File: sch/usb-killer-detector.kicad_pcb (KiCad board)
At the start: 2 copper layers, 44 x 82 mm, 35 parts, among them J1 USB_A, J2 USB_C_Receptacle_PowerOnly_6P, Q2 2N3904, U1 LM339

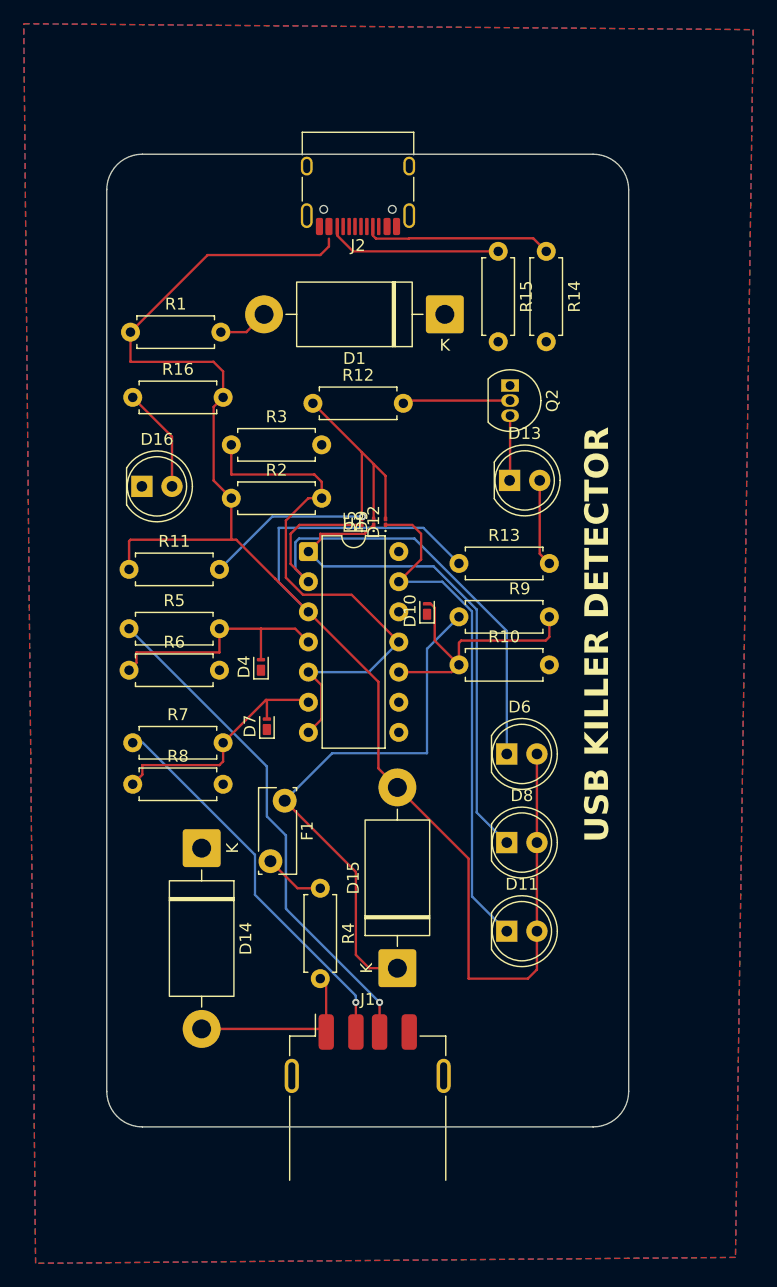
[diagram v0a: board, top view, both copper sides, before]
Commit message: Reprise v2 : schéma refait, PCB routé et dossier de fabrication
- Détection des deux polarités sur D+, D- et VBUS : comparateurs à
  fenêtre (2x LM339), seuils D+/D- +6,2 V / -5,0 V, VBUS +6,3 V / -0,3 V
- Alerte mémorisée (74HC279) avec bouton RESET et reset à la mise
  sous tension ; LED verte « OK » quand aucune alerte
- Protections : TVS SMAJ5.0A, clamps BAT54S, diode anti-retour SS34,
  polyfuse 500 mA
- PCB 44 x 82 mm entièrement routé, plans de masse sur les deux faces
- Règles d'isolation des lignes haute tension (kicad_dru) et classes
  de pistes (Power, HV)
- ERC 0, DRC 0 : les 2 avertissements de sérigraphie du connecteur
  USB-A (corps hors carte par construction) sont exclus avec justification
- sch/fabrication : Gerber + perçage (zip prêt à envoyer), BOM,
  fichier de placement, schéma et plan d'assemblage en PDF
- .gitignore : historique local de KiCad 10 (.history/)

Co-Authored-By: Claude Opus 5.5 <noreply@anthropic.com>
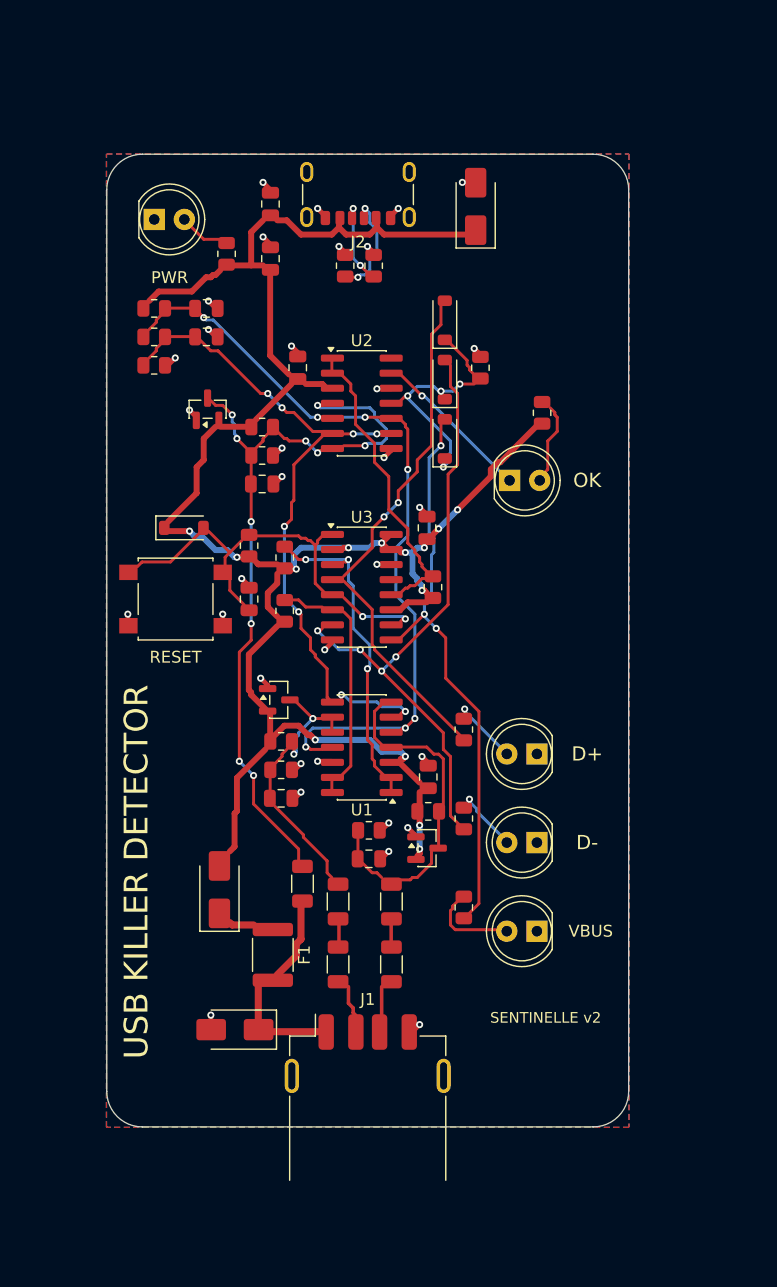
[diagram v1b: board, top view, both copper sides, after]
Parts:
- removed D16: LED_O, LED_THT:LED_D5.0mm
- removed Q2: 2N3904, Package_TO_SOT_THT:TO-92_Inline
- added C1: 10uF, Capacitor_SMD:C_0805_2012Metric, F.Cu at (80.3, 62.2)
- added C10: 100nF, Capacitor_SMD:C_0805_2012Metric, F.Cu at (93.5, 89.5)
- added C11: 1uF, Capacitor_SMD:C_0805_2012Metric, F.Cu at (78.5, 95.5)
- added C2: 100nF, Capacitor_SMD:C_0805_2012Metric, F.Cu at (80.3, 66.8)
- added C3: 100nF, Capacitor_SMD:C_0805_2012Metric, F.Cu at (74.9, 71.0)
- added C4: 100nF, Capacitor_SMD:C_0805_2012Metric, F.Cu at (74.9, 73.4)
- added C5: 1nF, Capacitor_SMD:C_0805_2012Metric, F.Cu at (88.6, 117.4)
- added C6: 1nF, Capacitor_SMD:C_0805_2012Metric, F.Cu at (81.2, 112.3)
- added C7: 1nF, Capacitor_SMD:C_0805_2012Metric, F.Cu at (79.6, 85.8)
- added C8: 100nF, Capacitor_SMD:C_0805_2012Metric, F.Cu at (93.6, 110.5)
- added C9: 100nF, Capacitor_SMD:C_0805_2012Metric, F.Cu at (82.6, 76.0)
- added D2: Orange PWR, LED_THT:LED_D5.0mm, F.Cu at (70.5, 63.5)
- added D3: SS34, Diode_SMD:D_SMA, F.Cu at (76.0, 120.0)
- added R17: 43k, Resistor_SMD:R_0805_2012Metric, F.Cu at (79.6, 83.4)
- added R18: 10k, Resistor_SMD:R_0805_2012Metric, F.Cu at (81.5, 92.0)
- added R19: 10k, Resistor_SMD:R_0805_2012Metric, F.Cu at (81.5, 96.5)
- added R20: 10k, Resistor_SMD:R_0805_2012Metric, F.Cu at (94.0, 94.5)
- added R21: 100k, Resistor_SMD:R_0805_2012Metric, F.Cu at (78.5, 91.0)
- added R22: 1k, Resistor_SMD:R_0805_2012Metric, F.Cu at (96.6, 106.5)
- added R23: 1k, Resistor_SMD:R_0805_2012Metric, F.Cu at (96.6, 114.0)
- added R24: 1k, Resistor_SMD:R_0805_2012Metric, F.Cu at (96.6, 121.5)
- added R25: 100k, Resistor_SMD:R_0805_2012Metric, F.Cu at (98.0, 76.0)
- added R26: 1k, Resistor_SMD:R_0805_2012Metric, F.Cu at (103.2, 79.8)
- added SW1: RESET, Button_Switch_SMD:SW_SPST_B3S-1000, F.Cu at (72.3, 95.5)
- added U2: LM339, Package_SO:SOIC-14_3.9x8.7mm_P1.27mm, F.Cu at (88.0, 79.0)
- added U3: 74HC279, Package_SO:SOIC-16_3.9x9.9mm_P1.27mm, F.Cu at (88.0, 94.5)
- D1: value D_Schottky -> SMAJ5.0A; footprint Diode_THT:D_DO-201AD_P15.24mm_Horizontal -> Diode_SMD:D_SMA
- D10: value PTVS7V5Z1USK -> Rouge D-; footprint Diode_SMD:Nexperia_DSN1608-2_1.6x0.8mm -> LED_THT:LED_D5.0mm
- D11: value LED_R_D- -> Rouge VBUS
- D12: value PTVS7V5Z1USK -> 1N4148W; footprint Diode_SMD:D_01005_0402Metric -> Diode_SMD:D_SOD-123
- D13: value LED_G -> 1N4148W; footprint LED_THT:LED_D5.0mm -> Diode_SMD:D_SOD-123
- D14: value D_Schottky -> 1N4148W; footprint Diode_THT:D_DO-201AD_P15.24mm_Horizontal -> Diode_SMD:D_SOD-123
- D15: value D_Schottky -> Verte OK; footprint Diode_THT:D_DO-201AD_P15.24mm_Horizontal -> LED_THT:LED_D5.0mm
- D4: value PTVS7V5Z1USK -> SMAJ5.0A; footprint Diode_SMD:Nexperia_DSN1608-2_1.6x0.8mm -> Diode_SMD:D_SMA
- D5: value PTVS7V5Z1USK -> BAT54S; footprint Diode_SMD:D_01005_0402Metric -> Package_TO_SOT_SMD:SOT-23
- D6: value LED_R_D+ -> BAT54S; footprint LED_THT:LED_D5.0mm -> Package_TO_SOT_SMD:SOT-23
- D7: value PTVS7V5Z1USK -> BAT54S; footprint Diode_SMD:Nexperia_DSN1608-2_1.6x0.8mm -> Package_TO_SOT_SMD:SOT-23
- D8: value LED_R_D- -> 1N4148W; footprint LED_THT:LED_D5.0mm -> Diode_SMD:D_SOD-123
- D9: value PTVS7V5Z1USK -> Rouge D+; footprint Diode_SMD:D_01005_0402Metric -> LED_THT:LED_D5.0mm
- F1: value Polyfuse 250-500mA -> 500mA hold; footprint Fuse:Fuse_Bourns_MF-RG300 -> Fuse:Fuse_1812_4532Metric
- J1: value USB_A -> USB-A test
- J2: value USB_C_Receptacle_PowerOnly_6P -> USB-C alim; footprint Connector_USB:USB_C_Receptacle_HRO_TYPE-C-31-M-12 -> Connector_USB:USB_C_Receptacle_GCT_USB4125-xx-x_6P_TopMnt_Horizontal
- R1: value 1K -> 5.1k; footprint Resistor_THT:R_Axial_DIN0207_L6.3mm_D2.5mm_P7.62mm_Horizontal -> Resistor_SMD:R_0805_2012Metric
- R10: value 22K -> 120k; footprint Resistor_THT:R_Axial_DIN0207_L6.3mm_D2.5mm_P7.62mm_Horizontal -> Resistor_SMD:R_0805_2012Metric
- R11, R7: value 100K -> 220k; footprint Resistor_THT:R_Axial_DIN0207_L6.3mm_D2.5mm_P7.62mm_Horizontal -> Resistor_SMD:R_1206_3216Metric
- R12: value 47K -> 220k; footprint Resistor_THT:R_Axial_DIN0207_L6.3mm_D2.5mm_P7.62mm_Horizontal -> Resistor_SMD:R_1206_3216Metric
- R13: value 100K -> 220k; footprint Resistor_THT:R_Axial_DIN0207_L6.3mm_D2.5mm_P7.62mm_Horizontal -> Resistor_SMD:R_0805_2012Metric
- R14: value 5k -> 120k; footprint Resistor_THT:R_Axial_DIN0207_L6.3mm_D2.5mm_P7.62mm_Horizontal -> Resistor_SMD:R_0805_2012Metric
- R15: value 5k -> 100k; footprint Resistor_THT:R_Axial_DIN0207_L6.3mm_D2.5mm_P7.62mm_Horizontal -> Resistor_SMD:R_1206_3216Metric
- R16: value 10K -> 150k; footprint Resistor_THT:R_Axial_DIN0207_L6.3mm_D2.5mm_P7.62mm_Horizontal -> Resistor_SMD:R_0805_2012Metric
- R2: value 36K -> 5.1k; footprint Resistor_THT:R_Axial_DIN0207_L6.3mm_D2.5mm_P7.62mm_Horizontal -> Resistor_SMD:R_0805_2012Metric
- R3: value 10K -> 1k; footprint Resistor_THT:R_Axial_DIN0207_L6.3mm_D2.5mm_P7.62mm_Horizontal -> Resistor_SMD:R_0805_2012Metric
- R4: value 22 -> 51k; footprint Resistor_THT:R_Axial_DIN0207_L6.3mm_D2.5mm_P7.62mm_Horizontal -> Resistor_SMD:R_0805_2012Metric
- R5: value 100K -> 33k; footprint Resistor_THT:R_Axial_DIN0207_L6.3mm_D2.5mm_P7.62mm_Horizontal -> Resistor_SMD:R_0805_2012Metric
- R6: value 22K -> 15k; footprint Resistor_THT:R_Axial_DIN0207_L6.3mm_D2.5mm_P7.62mm_Horizontal -> Resistor_SMD:R_0805_2012Metric
- R8: value 22K -> 220k; footprint Resistor_THT:R_Axial_DIN0207_L6.3mm_D2.5mm_P7.62mm_Horizontal -> Resistor_SMD:R_1206_3216Metric
- R9: value 390K -> 220k; footprint Resistor_THT:R_Axial_DIN0207_L6.3mm_D2.5mm_P7.62mm_Horizontal -> Resistor_SMD:R_0805_2012Metric
- U1: footprint Package_DIP:DIP-14_W7.62mm -> Package_SO:SOIC-14_3.9x8.7mm_P1.27mm
- moved R15 55.8 mm to (83.0, 119.5), turned to 90 degrees
- moved R4 50.8 mm to (70.5, 71.0), turned to 0 degrees
- moved R14 49.1 mm to (81.2, 109.9), turned to 0 degrees
- moved D15 42.2 mm to (100.5, 85.5), turned to 0 degrees
- moved R12 42.1 mm to (86.0, 121.0), turned to 90 degrees
- moved D14 40.1 mm to (95.0, 82.0), turned to 90 degrees
- moved D8 38.0 mm to (73.0, 89.5)
- moved R11 37.7 mm to (86.0, 126.3), turned to 90 degrees
- moved D4 30.7 mm to (77.3, 131.8), turned to 180 degrees
- moved R7 28.7 mm to (90.5, 126.3), turned to 90 degrees
- moved D5 28.0 mm to (93.5, 116.5), turned to 0 degrees
- moved D7 27.2 mm to (75.0, 79.5)
- moved R6 25.8 mm to (70.5, 75.8)
- moved R5 24.7 mm to (70.5, 73.4)
- moved R8 23.9 mm to (90.5, 121.0), turned to 90 degrees
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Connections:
- D1 pad 1: GND -> +5V
- D1 pad 2: Net-(D1-A) -> GND
- D10 pad 2: Net-(D10-A) -> /LED_DM
- D11 pad 1: Net-(D11-K) -> GND
- D11 pad 2: 5V -> /LED_VBUS
- D12 pad 1: Net-(D11-K) -> /ANY_ALM
- D12 pad 2: Net-(D12-A) -> /Q_DP
- D13 pad 1: Net-(D13-K) -> /ANY_ALM
- D13 pad 2: Net-(D13-A) -> /Q_DM
- D14 pad 1: GND -> /ANY_ALM
- D14 pad 2: VBUS -> /Q_VBUS
- D15 pad 1: VBUS_TEST -> /LED_OK_K
- D15 pad 2: 5V -> /LED_OK_A
- D4 pad 1: GND -> /VBUS_PORT
- D4 pad 2: Net-(D4-A) -> GND
- D5 pad 1: Net-(D5-K) -> GND
- D5 pad 2: Net-(D12-A) -> +5V
- D6 pad 1: Net-(D5-K) -> GND
- D6 pad 2: 5V -> +5V
- D7 pad 2: Net-(D7-A) -> +5V
- D8 pad 1: Net-(D8-K) -> +5V
- D8 pad 2: 5V -> /RST_N
- D9 pad 1: Net-(D8-K) -> GND
- D9 pad 2: Net-(D12-A) -> /LED_DP
- F1 pad 1: VBUS_TEST -> /VBUS_SRC
- F1 pad 2: Net-(F1-Pad2) -> /VBUS_PORT
- J1 pad 1: VBUS -> /VBUS_PORT
- J1 pad 2: D- -> /DM
- J1 pad 3: D+ -> /DP
- J1 pad SH: unconnected-(J1-Shield-PadSH) -> GND
- J2 pad A5: Net-(J2-CC1) -> /CC1
- J2 pad A9: 5V -> +5V
- J2 pad B5: Net-(J2-CC2) -> /CC2
- J2 pad B9: 5V -> +5V
- J2 pad SH: unconnected-(J2-SHIELD-PadSH) -> GND
- R1 pad 1: 5V -> /CC1
- R1 pad 2: Net-(D1-A) -> GND
- R10 pad 1: Net-(D10-A) -> /X_DP
- R11 pad 1: 5V -> /DM
- R11 pad 2: Net-(D12-A) -> /DM_HV
- R12 pad 1: Net-(D12-A) -> /DM_HV
- R12 pad 2: Net-(Q2-B) -> /X_DM
- R13 pad 1: 5V -> +5V
- R13 pad 2: Net-(D13-A) -> /X_DM
- R14 pad 1: Net-(J2-CC1) -> /X_DM
- R15 pad 1: Net-(J2-CC2) -> /VBUS_PORT
- R15 pad 2: GND -> /X_VBUS
- R16 pad 1: Net-(D16-A) -> +5V
- R16 pad 2: 5V -> /X_VBUS
- R2 pad 1: 5V -> /CC2
- R2 pad 2: VREF -> GND
- R3 pad 1: VREF -> +5V
- R3 pad 2: GND -> /LED_PWR
- R4 pad 1: Net-(F1-Pad2) -> +5V
- R4 pad 2: VBUS -> /VH
- R5 pad 1: D+ -> /VH
- R5 pad 2: Net-(D4-A) -> /VL
- R6 pad 1: Net-(D4-A) -> /VL
- R7 pad 1: D- -> /DP
- R7 pad 2: Net-(D7-A) -> /DP_HV
- R8 pad 1: Net-(D7-A) -> /DP_HV
- R8 pad 2: GND -> /X_DP
- R9 pad 1: VBUS_TEST -> +5V
- R9 pad 2: Net-(D10-A) -> /X_DP
- U1 pad 1: Net-(D8-K) -> /ALM_DP_N
- U1 pad 10: Net-(D10-A) -> /X_DM
- U1 pad 11: VREF -> /VH
- U1 pad 13: Net-(D11-K) -> /ALM_DM_N
- U1 pad 14: (no net) -> /ALM_DM_N
- U1 pad 2: Net-(D5-K) -> /ALM_DP_N
- U1 pad 3: 5V -> +5V
- U1 pad 4: Net-(D4-A) -> /X_DP
- U1 pad 5: VREF -> /VH
- U1 pad 6: Net-(D7-A) -> /VL
- U1 pad 7: VREF -> /X_DP
- U1 pad 8: (no net) -> /VL
- U1 pad 9: (no net) -> /X_DM
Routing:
- net 5V: track 151.5 -> 0.00 mm
- net +5V: track 0.00 -> 144.4 mm, vias 0 -> 14
- net /VH: track 0.00 -> 61.9 mm, vias 0 -> 7
- net /X_VBUS: track 0.00 -> 58.6 mm, vias 0 -> 10
- net /VL: track 0.00 -> 52.0 mm, vias 0 -> 8
- net /Q_DM: track 0.00 -> 51.7 mm, vias 0 -> 4
- net VREF: track 47.5 -> 0.00 mm
- net /Q_VBUS: track 0.00 -> 47.2 mm, vias 0 -> 3
- net Net-(D5-K): track 46.3 -> 0.00 mm, vias 1 -> 0
- net VBUS_TEST: track 45.7 -> 0.00 mm
- net Net-(D8-K): track 43.6 -> 0.00 mm, vias 1 -> 0
- net Net-(D11-K): track 43.5 -> 0.00 mm, vias 1 -> 0
- net /Q_DP: track 0.00 -> 43.3 mm, vias 0 -> 2
- net D+: track 42.7 -> 0.00 mm, vias 1 -> 0
- net Net-(D12-A): track 36.5 -> 0.00 mm, vias 1 -> 0
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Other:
- board text added: "D+"
- board text added: "D-"
- board text added: "OK"
- board text added: "PWR"
- board text added: "RESET"
- board text added: "SENTINELLE v2"
- board text added: "VBUS"
